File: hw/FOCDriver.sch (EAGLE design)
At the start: 108 parts, among them Q1 BC546B, Q2 BC546B, Q3 BC546B, Q4 BC546B, Q5 BC546B, Q6 BC546B, U4 IRF9389TRPBF, U5 IRF9389TRPBF, U6 IRF9389TRPBF, U7 LM27313XMF, U8 LM358N, U9 LM358N

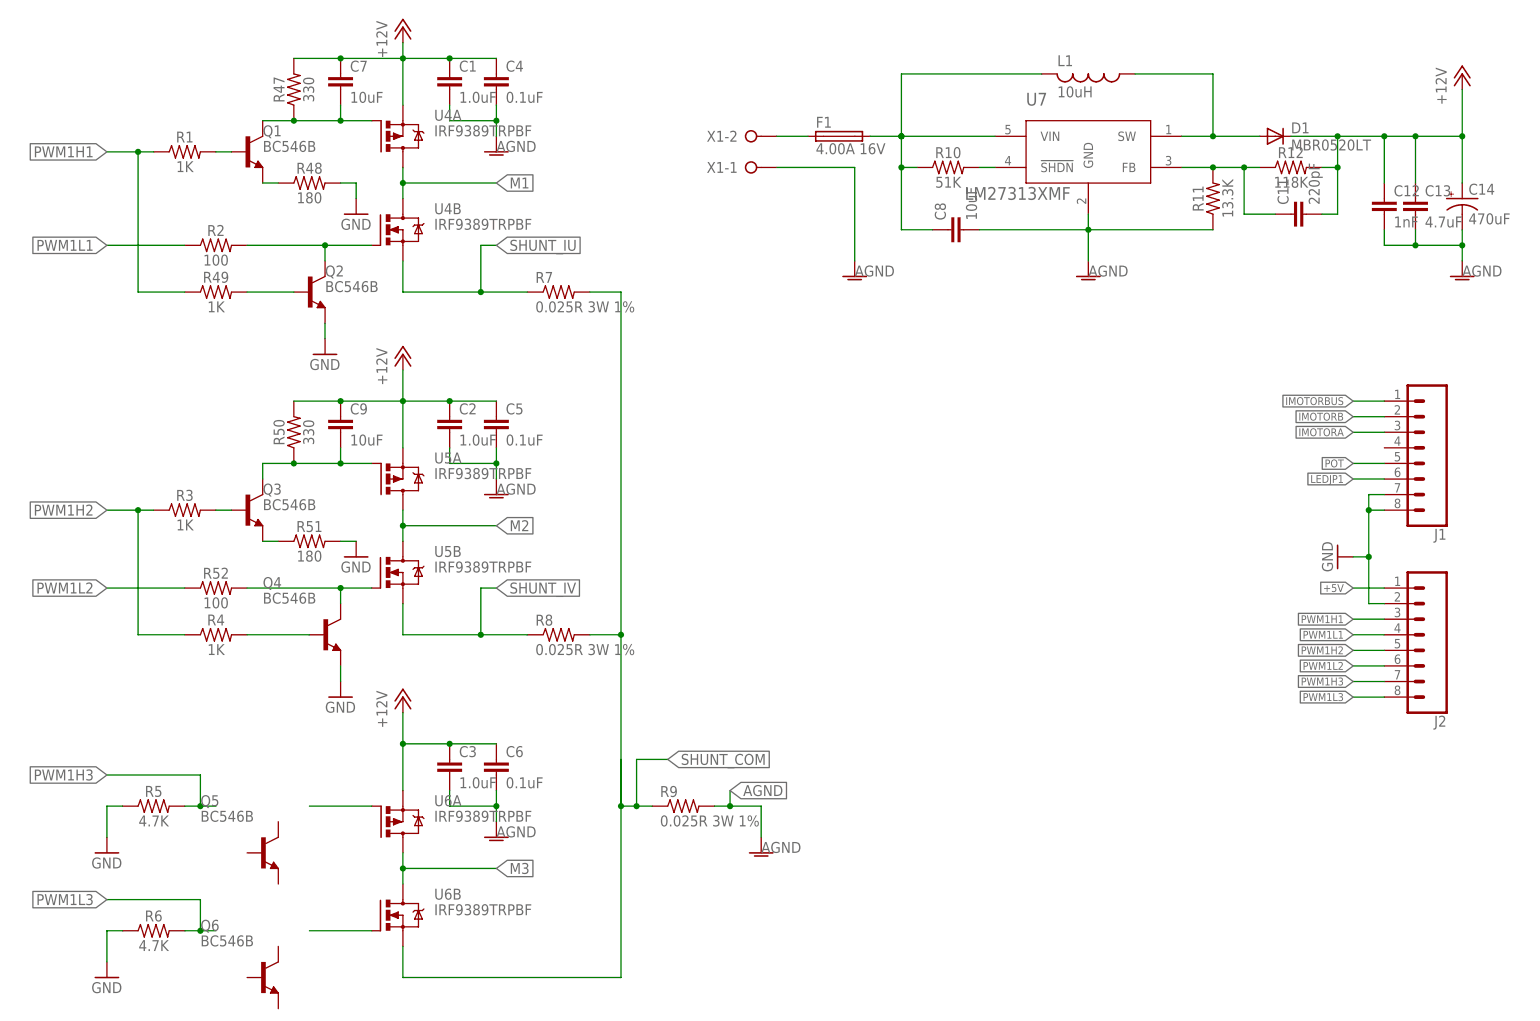
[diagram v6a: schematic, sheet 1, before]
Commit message: layout trans driver
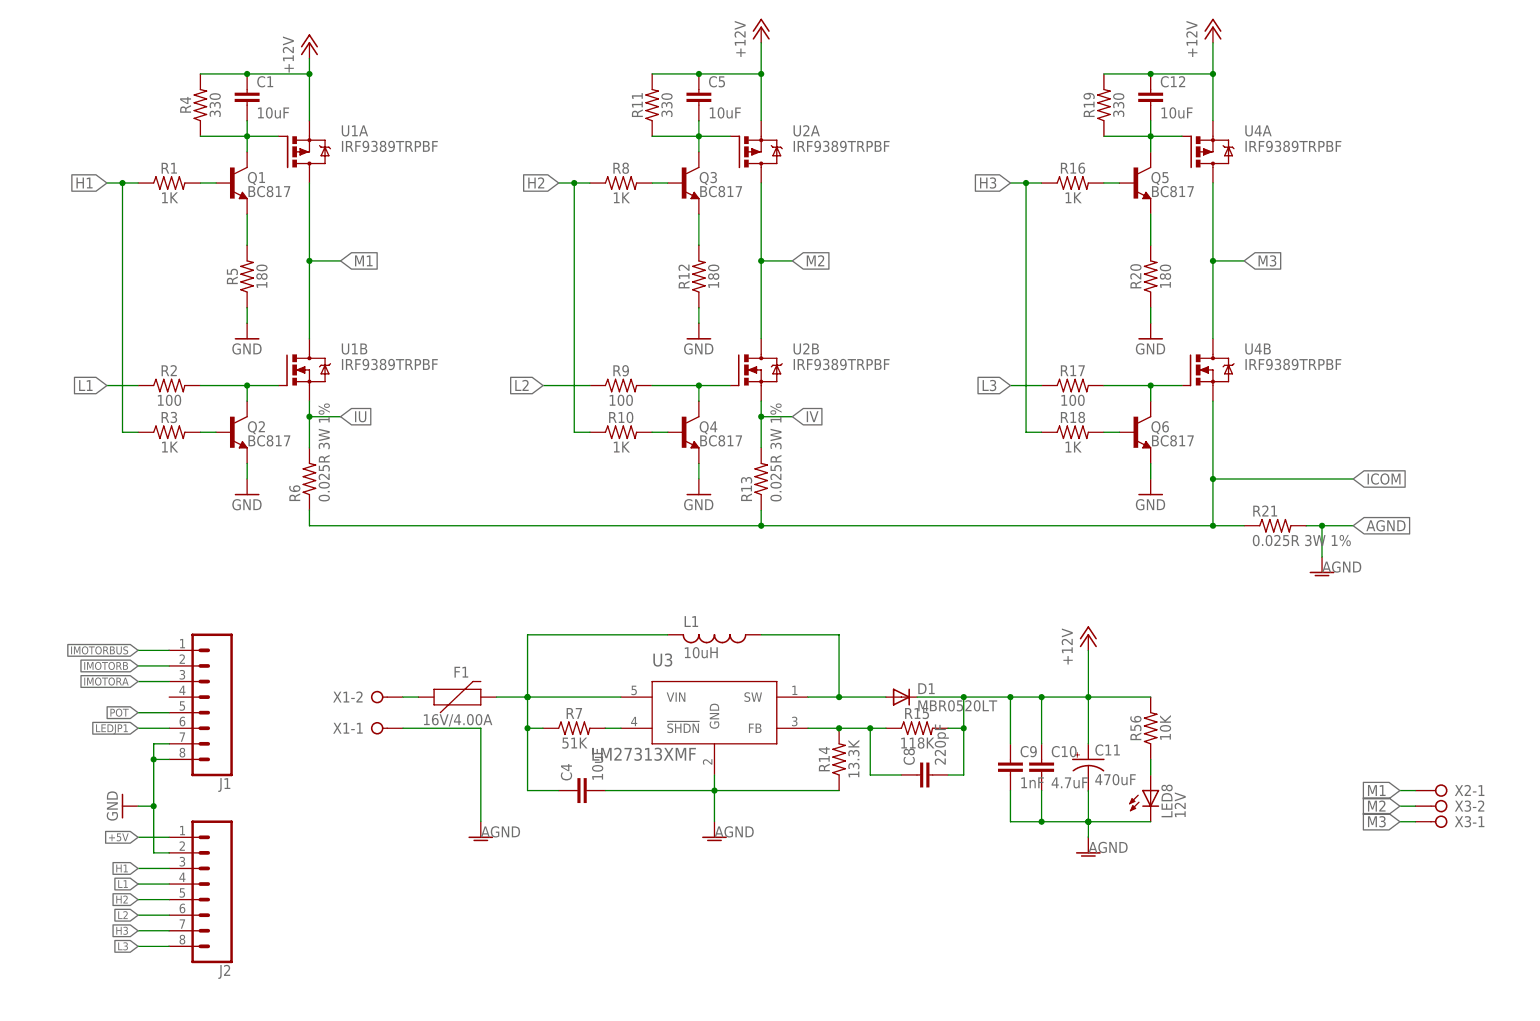
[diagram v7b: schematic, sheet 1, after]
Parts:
- removed C13: 4.7uF, SparkFun-Capacitors:1.0UF-0805-25V-10%
- removed C14: 470uF, rcl:CPOL-USE2.5-7
- removed C2, C3: 1.0uF, SparkFun-Capacitors:1.0UF-0805-25V-10%
- removed C6: 0.1uF, SparkFun-Capacitors:1.0UF-0805-25V-10%
- removed C7: 10uF, SparkFun-Capacitors:1.0UF-0805-25V-10%
- removed U7: LM27313XMF, LM27313XMF:LM27313XMF
- removed U8, U9: LM358N, Fairchild-LM358N:LM358N
- added C10: 4.7uF, SparkFun-Capacitors:1.0UF-0805-25V-10%
- added LED8: 12V, led:LEDSML0805
- added R53: 3.3K, SparkFun-Resistors:RESISTOR0805
- added R54: (no value), pot:TRIM_US-CT6
- added R55: 1K, SparkFun-Resistors:RESISTOR0805
- added R56: 10K, SparkFun-Resistors:RESISTOR0805
- added U1, U2: IRF9389TRPBF, IRF9389TRPBF:IRF9389TRPBF
- added U3: LM27313XMF, LM27313XMF:LM27313XMF
- C1: value 1.0uF -> 10uF
- C11: value 220pF -> 470uF; device SparkFun-Capacitors:1.0UF-0805-25V-10% -> rcl:CPOL-USE2.5-7
- C12: value 1nF -> 10uF
- C4, C5: value 0.1uF -> 10uF
- C8: value 10uF -> 220pF
- C9: value 10uF -> 1nF
- F1: value 4.00A 16V -> 16V/4.00A; device fuse:TE5 -> SparkFun-Fuses:PPTC_PTH
- LED7: value (none) -> 5V
- Q1, Q2, Q3, Q4, Q5, Q6: value BC546B -> BC817; device transistor-npn:BC546B -> SparkFun-DiscreteSemi:TRANS_NPN-MMBT2222AL
- R10: value 51K -> 1K
- R11: value 13.3K -> 330
- R12: value 118K -> 180
- R13, R21: value 1K 1% -> 0.025R 3W 1%; device SparkFun-Resistors:RESISTOR0805 -> resistor:R-US_R2512
- R14: value 1K 1% -> 13.3K
- R15: value 1K 1% -> 118K
- R16, R18: value 1K 1% -> 1K
- R17: value 1K 1% -> 100
- R19: value 1K 1% -> 330
- R20: value 1K 1% -> 180
- R25, R26: value 51K -> 1K 1%
- R27, R28, R29, R30, R31, R32: value 30K 1% -> 1K 1%
- R34, R35: value 1K 1% -> 30K 1%
- R36, R37, R40, R41: value 1K -> 30K 1%
- R38: value 1R -> 30K 1%
- R39: value 0R -> 30K 1%
- R4: value 1K -> 330
- R42, R43: value 1K -> 1K 1%
- R44: value 3.3K -> 1K 1%
- R45: value (none) -> 1K; device pot:TRIM_US-CT6 -> SparkFun-Resistors:RESISTOR0805
- R47: value 330 -> 1R
- R48: value 180 -> 0R
- R5: value 4.7K -> 180
- R50: value 330 -> 1K
- R51: value 180 -> 1K
- R52: value 100 -> 1K
- R6: value 4.7K -> 0.025R 3W 1%; device SparkFun-Resistors:RESISTOR0805 -> resistor:R-US_R2512
- R7: value 0.025R 3W 1% -> 51K; device resistor:R-US_R2512 -> SparkFun-Resistors:RESISTOR0805
- R8: value 0.025R 3W 1% -> 1K; device resistor:R-US_R2512 -> SparkFun-Resistors:RESISTOR0805
- R9: value 0.025R 3W 1% -> 100; device resistor:R-US_R2512 -> SparkFun-Resistors:RESISTOR0805
- U5, U6: value IRF9389TRPBF -> LM358N; device IRF9389TRPBF:IRF9389TRPBF -> Fairchild-LM358N:LM358N
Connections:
- removed net PWM1H1: J2.3, R1.1, R36.2, R49.1
- removed net PWM1H2: J2.5, R3.1, R4.1, R40.2
- removed net PWM1H3: J2.7, R42.2, R5.2
- removed net PWM1L1: J2.4, R2.1, R37.2
- removed net PWM1L2: J2.6, R41.2, R52.1
- removed net PWM1L3: J2.8, R43.2, R6.2
- removed net SHUNT_COM: R13.1, R15.1, R18.1, R7.2, R8.2, R9.1, U6B.S
- removed net SHUNT_IU: R14.1, R7.1, U4B.S
- removed net SHUNT_IV: R16.1, R8.1, U5B.S
- new net H1: J2.3, R1.1, R3.1, R45.2
- new net H2: J2.5, R10.1, R49.2, R8.1
- new net H3: J2.7, R16.1, R18.1, R51.2
- new net ICOM: R13.1, R21.1, R22.1, R24.1, R27.1, R6.1, U4B.S
- new net IU: R23.1, R6.2, U1B.S
- new net IV: R13.2, R25.1, U2B.S
- new net L1: J2.4, R2.1, R46.2
- new net L2: J2.6, R50.2, R9.1
- new net L3: J2.8, R17.1, R52.2
- new net N$42: Q5.B, R16.2
- new net N$43: Q3.E, R12.2
- new net N$44: Q6.B, R18.2
- new net N$45: LED8.A, R56.1
- net +12V: now also C10.1, C11.+, C8.2, R11.2, R15.2, R19.2, R4.2, R56.2, U1A.S, U2A.S; no longer C11.2, C13.1, C14.+, C2.1, C3.1, C4.1, C6.1, C7.1, R12.2, R47.2, R50.2, U5A.S, U6A.S
- net +5V: now also R47.1, R53.2, R54.E; no longer R38.1, R44.2, R45.E
- net AGND: now also C10.2, C11.-, C9.2, LED8.C, R14.1, R21.2, R35.1, R48.2, U3.GND, U5G$3.GND, U6G$3.GND; no longer C1.2, C12.2, C13.2, C14.-, C2.2, C3.2, C5.2, C6.2, C8.2, R11.1, R17.1, R39.2, R9.2, U7.GND, U8G$3.GND, U9G$3.GND
- net AVDD: now also R34.2, R47.2, U5G$3.VCC, U6G$3.VCC; no longer R25.2, R38.2, U8G$3.VCC, U9G$3.VCC
- net GND: now also Q6.E, R12.1, R20.1, R48.1, R55.1; no longer R39.1, R46.1, R48.2, R51.2, R6.1
- net IMOTORA: now also R42.2; no longer R33.2
- net IMOTORB: now also R43.2; no longer R34.2
- net IMOTORBUS: now also R44.2; no longer R35.2
- net M1: now also U1A.D, U1B.D; no longer U4A.D, U4B.D
- net M2: now also U2A.D, U2B.D; no longer U5A.D, U5B.D
- net M3: now also U4A.D, U4B.D; no longer U6A.D, U6B.D
- net N$1: now also C4.1, R7.1, U3.VIN; no longer C8.1, R10.1, U7.VIN
- net N$10: now also C1.2, R4.1, U1A.G; no longer C7.2, R47.1, U4A.G
- net N$11: now also R22.2, R28.1; no longer R13.2, R19.1
- net N$12: now also R23.2, R29.1; no longer R14.2, R20.1
- net N$13: now also R28.2, R36.1, U5G$2.-IN; no longer R19.2, R27.1, U8G$2.-IN
- net N$14: now also R24.2, R30.1; no longer R15.2, R21.1
- net N$15: now also R29.2, R39.1, U5G$2.+IN; no longer R20.2, R30.1, U8G$2.+IN
- net N$16: now also R36.2, R42.1, U5G$2.OUT; no longer R27.2, R33.1, U8G$2.OUT
- net N$17: now also R25.2, R31.1; no longer R16.2, R22.1
- net N$18: now also R34.1, R35.2, U6G$2.+IN; no longer R25.1, R26.2, U9G$2.+IN
- net N$19: now also R30.2, R37.1, U5G$1.-IN; no longer R21.2, R28.1, U8G$1.-IN
- net N$2: now also R7.2, U3.!SHDN!; no longer R10.2, U7.!SHDN!
- net N$20: now also R31.2, R40.1, U5G$1.+IN; no longer R22.2, R31.1, U8G$1.+IN
- net N$21: now also R37.2, R43.1, U5G$1.OUT; no longer R28.2, R34.1, U8G$1.OUT
- net N$22: now also R26.2, R32.1; no longer R17.2, R23.1
- net N$23: now also R27.2, R33.1; no longer R18.2, R24.1
- net N$24: now also R32.2, R38.1, U6G$1.-IN; no longer R23.2, R29.1, U9G$1.-IN
- net N$25: now also R33.2, R41.1, U6G$1.+IN; no longer R24.2, R32.1, U9G$1.+IN
- net N$26: now also R38.2, R44.1, U6G$1.OUT; no longer R29.2, R35.1, U9G$1.OUT
- net N$28: now also Q5.E, R20.2; no longer Q1.E, R48.1
- net N$29: now also R54.A, R55.2; no longer R45.A, R46.2
- net N$3: now also Q6.C, R17.2, U4B.G; no longer U6B.G
- net N$31: now also R53.1; no longer R44.1
- net N$32: now also R3.2; no longer R49.2
- net N$33: now also R45.1; no longer R36.1
- net N$34: now also R46.1; no longer R37.1
- net N$35: now also R49.1; no longer R40.1
- net N$36: now also R50.1; no longer R41.1
- net N$37: now also R51.1; no longer R42.1
- net N$38: now also R52.1; no longer R43.1
- net N$39: now also R8.2; no longer R3.2
- net N$4: now also C8.1, R14.2, R15.1, U3.FB; no longer C11.1, R11.2, R12.1, U7.FB
- net N$40: now also Q1.E, R5.2; no longer Q3.E, R51.1
- net N$41: now also R10.2; no longer R4.2
- net N$5: now also U3.SW; no longer U7.SW
- net N$6: now also C12.2, Q5.C, R19.1, U4A.G; no longer U6A.G
- net N$7: now also R9.2, U2B.G; no longer R52.2, U5B.G
- net N$8: now also C5.2, R11.1, U2A.G; no longer C9.2, R50.1, U5A.G
- net N$9: now also U1B.G; no longer U4B.G
- net POT: now also R54.S; no longer R45.S
- net VREF: now also R39.2, R40.2, R41.2, U6G$2.-IN, U6G$2.OUT; no longer R30.2, R31.2, R32.2, U9G$2.-IN, U9G$2.OUT
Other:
- moved on the sheet: C1, C12, C4, C5, C8, C9, D1, J1, J2, L1, Q1, Q2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

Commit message: simulation
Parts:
- added U7, U8, U9: SN74LVC1G17, SN74LVC1G17:SN74LVC1G17
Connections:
- new net N$46: R2.1, U7.Y
- new net N$47: R9.1, U8.Y
- new net N$48: R17.1, U9.Y
- net +5V: now also U7.VCC, U8.VCC, U9.VCC
- net GND: now also U7.GND, U8.GND, U9.GND
- net L1: now also U7.A; no longer R2.1
- net L2: now also U8.A; no longer R9.1
- net L3: now also U9.A; no longer R17.1
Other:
- moved on the sheet: R10, R17, R18, R2, R3, R9
